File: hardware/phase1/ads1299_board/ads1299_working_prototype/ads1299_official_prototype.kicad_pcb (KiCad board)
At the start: 4 copper layers, 106 parts, among them J2 1725656, J3 TSM-110-01-T-DV-P-TR, J6 36PIN_IDC, J80 Conn_02x16_Odd_Even, J81 Conn_02x16_Odd_Even, J9 1725656, U1 ADS1299IPAG, U10 24AA256-I/ST, U11 OPA376AID, U4 OPA376

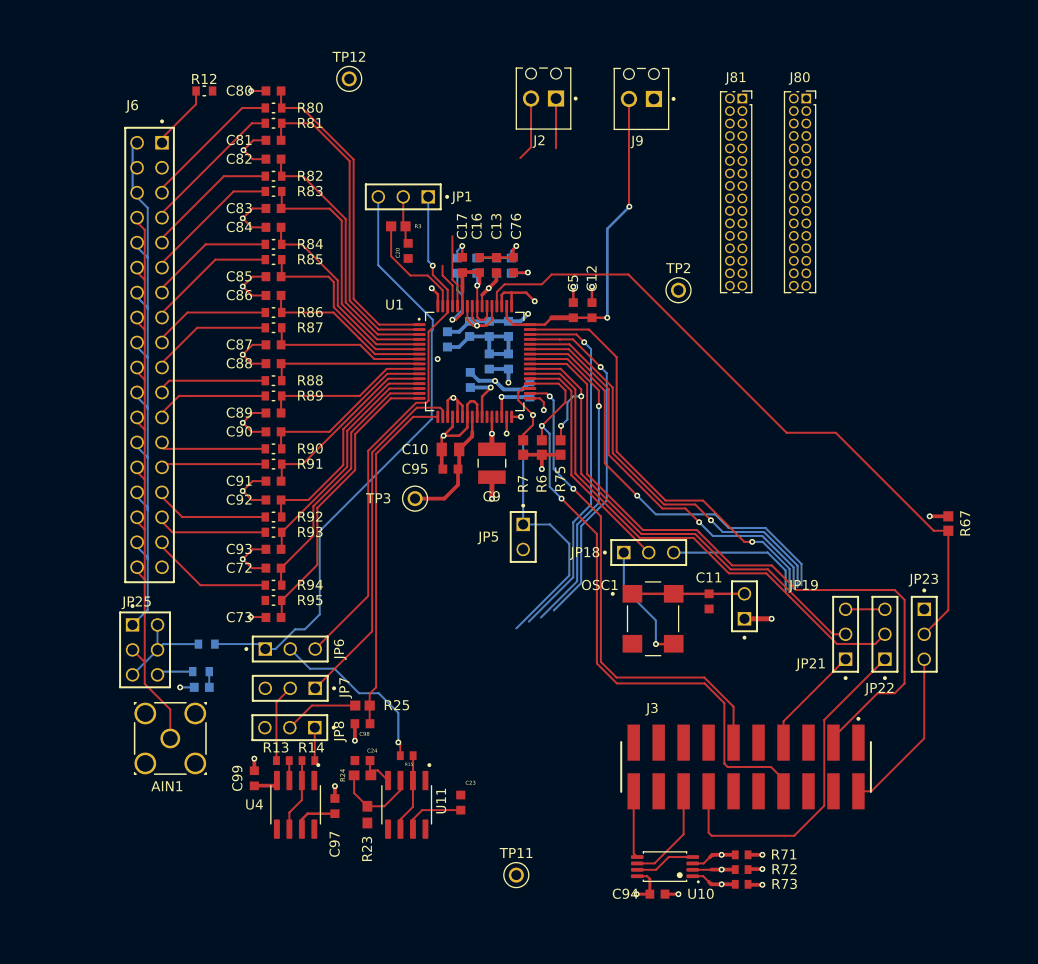
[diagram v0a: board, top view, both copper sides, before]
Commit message: Only thing left is the AVDD power routing, not sure if we can just connect that to power plane or not. Also ground plane, then done
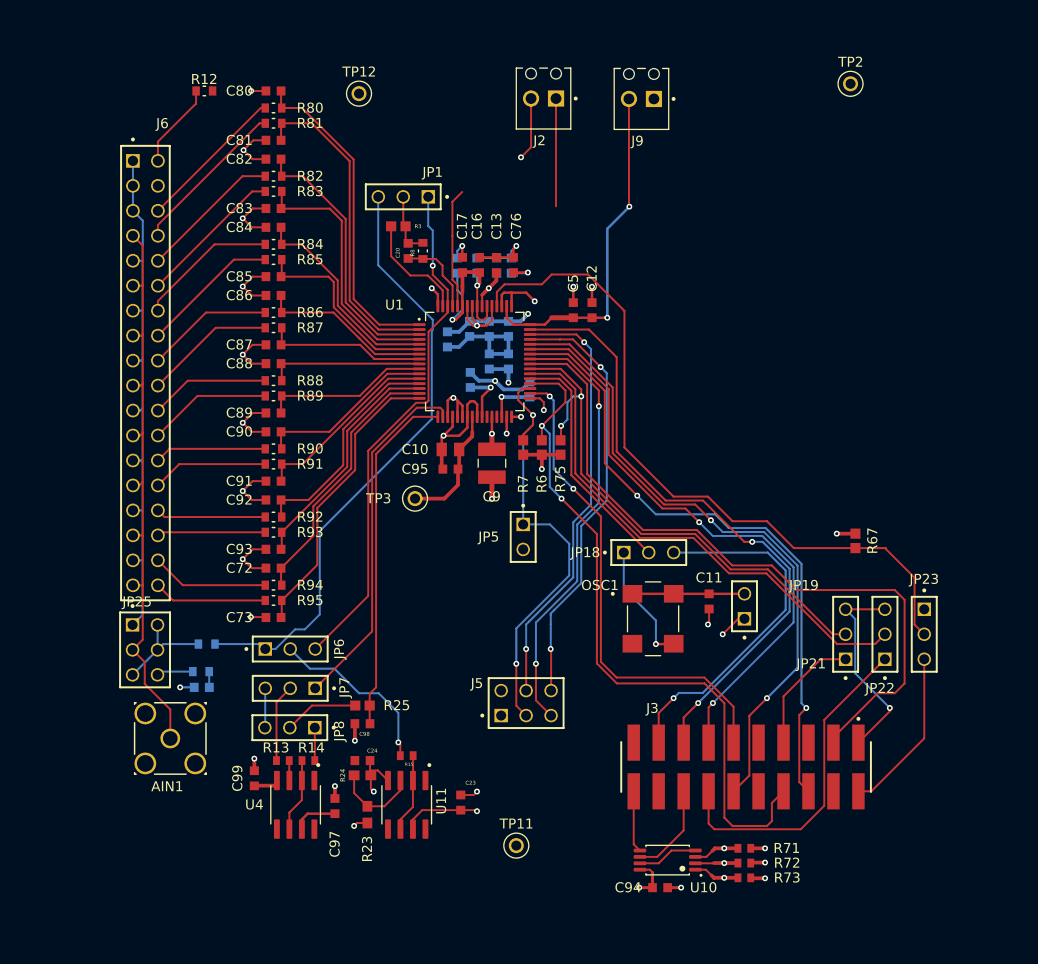
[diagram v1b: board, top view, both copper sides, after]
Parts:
- removed J80, J81: Conn_02x16_Odd_Even, Connector_PinSocket_1.27mm:PinSocket_2x16_P1.27mm_Vertical
- added J5: TSW-103-07-T-D, TSW-103-07-T-D:SAMTEC_TSW-103-07-T-D, F.Cu at (141.0, 109.5)
- added R8: 392K, RC0603FR-07392KL:RESC1608X55N, F.Cu at (130.5, 63.5)
- moved TP2 27.3 mm to (174.0, 46.5)
- moved R67 9.61 mm to (174.5, 93.0)
- moved TP11 3.00 mm to (140.0, 124.0)
- moved J6 2.42 mm to (102.4, 54.3)
- moved TP12 1.80 mm to (124.0, 47.5)
- moved U10 0.72 mm to (155.4, 125.5)
- moved C94 0.72 mm to (154.6, 128.3)
- moved R71 0.72 mm to (163.2, 124.3)
- moved R72 0.72 mm to (163.2, 125.8)
- moved R73 0.72 mm to (163.2, 127.3)
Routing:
- net GPIO2: track 42.6 -> 66.1 mm, vias 1 -> 2
- net EXT_CLK: track 14.3 -> 36.4 mm, vias 0 -> 1
- net GPIO1: track 42.9 -> 64.8 mm, vias 1 -> 2
- net SPI_DRDY: track 44.3 -> 64.3 mm, vias 1 -> 2
- net SPI_OUT: track 42.1 -> 61.3 mm, vias 1 -> 2
- net Net-(J3-Pad01): track 4.00 -> 20.8 mm, vias 0 -> 1
- net 36: track 0.00 -> 11.6 mm
- net 1: track 66.4 -> 55.3 mm
- net DAISY_IN: track 33.9 -> 44.7 mm, vias 1 -> 2
- net /PWDN: track 35.2 -> 44.4 mm, vias 1 -> 2
- net GPIO3: track 35.6 -> 43.9 mm, vias 1 -> 2
- net /RESET: track 66.2 -> 73.9 mm
- net AVSS: track 61.4 -> 69.1 mm, vias 7 -> 8
- net 11: track 68.6 -> 61.0 mm
- net GPIO4: track 37.2 -> 44.3 mm, vias 1 -> 2
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
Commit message: Planes are in, need to ask bruno on specifics about them then done
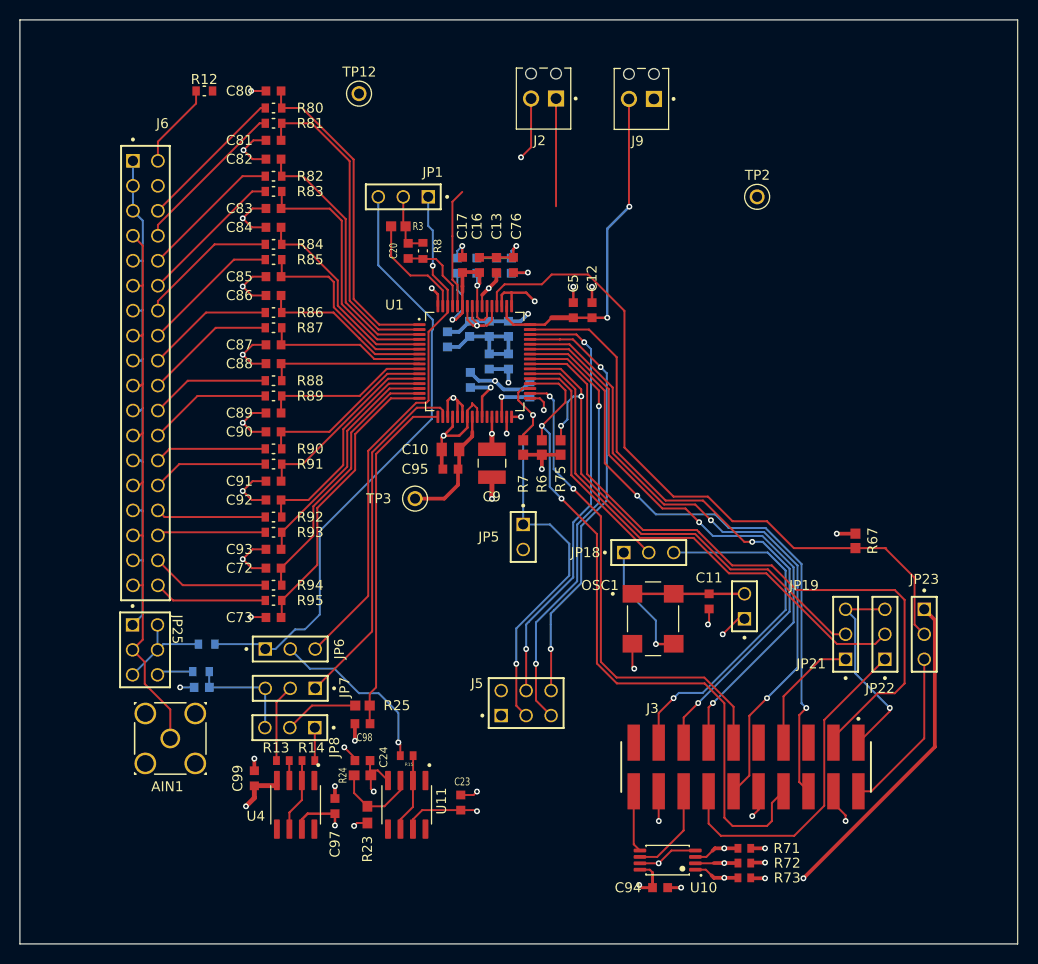
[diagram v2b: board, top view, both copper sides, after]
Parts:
- removed TP11: 5001, 5001:KEYSTONE_5001
- moved TP2 14.9 mm to (164.5, 58.0)
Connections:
- C94 pad 1: +3V3 -> DVDD
- R71 pad 2: +3V3 -> DVDD
- R72 pad 2: +3V3 -> DVDD
- R73 pad 2: +3V3 -> DVDD
- U10 pad 1: +3V3 -> DVDD
- U10 pad 2: +3V3 -> DVDD
- U10 pad 3: +3V3 -> DVDD
- U10 pad 8: +3V3 -> DVDD
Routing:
- net GND: track 11.9 -> 45.3 mm, vias 4 -> 6
- net DVDD: track 45.3 -> 63.4 mm, vias 5 -> 9
- net +3V3: track 18.0 -> 0.00 mm, vias 4 -> 0
- net GNDA: track 75.0 -> 89.0 mm, vias 24 -> 29
- net REF_ELEC: track 5.62 -> 11.4 mm
- net AVSS: track 69.1 -> 70.9 mm, vias 8 -> 9
- net AVDD: track 59.9 -> 61.1 mm, vias 6 -> 7
- net Net-(J3-Pad14): track 33.7 -> 34.3 mm
- added copper zone on In2.Cu, net DVDD
- added copper zone on In1.Cu, net GND
- added copper zone on In1.Cu, net GNDA
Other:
- board outline added: 101.5 x 94 mm

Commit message: DONE, but need to edit some footprints and add the biasref header
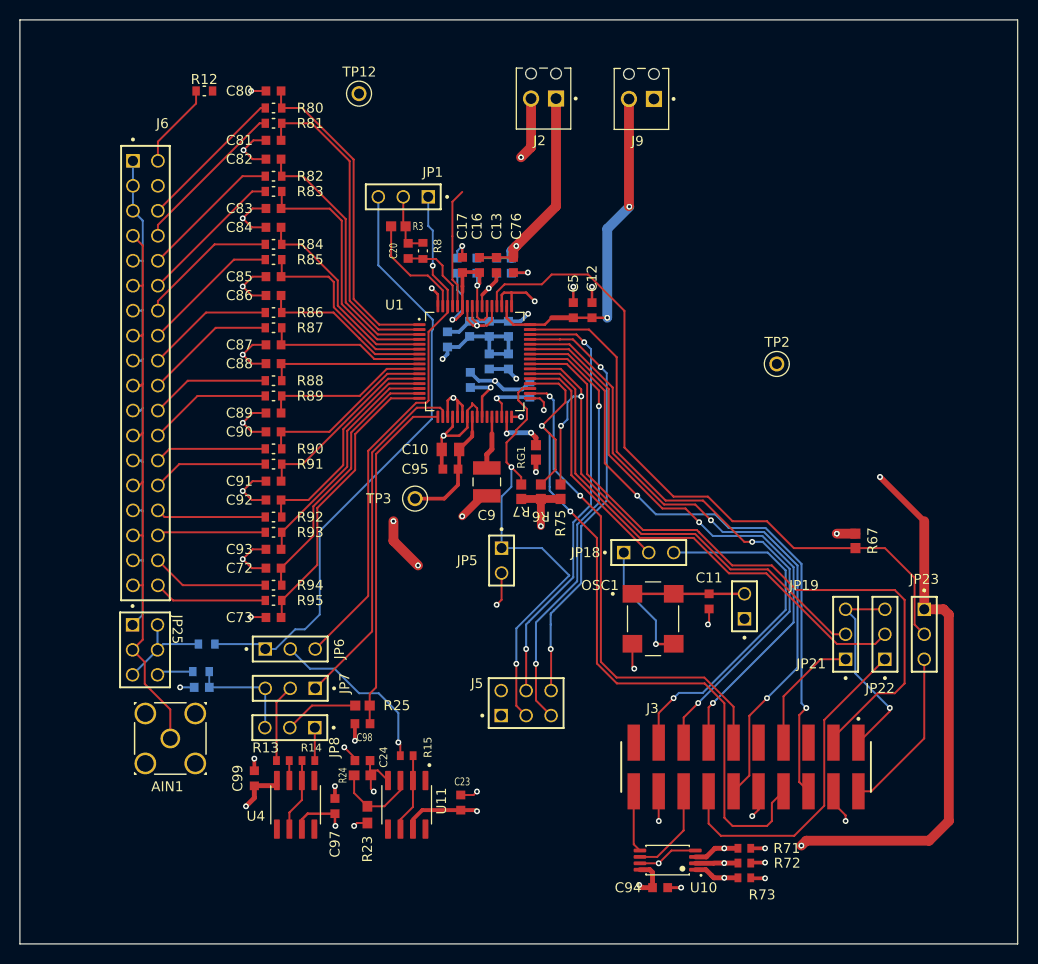
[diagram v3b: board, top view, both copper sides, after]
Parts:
- added RG1: 0, RC0603JR-070RL:RESC1607X60N, F.Cu at (142.0, 84.0)
- moved TP2 17.1 mm to (166.5, 75.0)
- moved R7 4.50 mm to (140.5, 88.0)
- moved R6 4.50 mm to (142.5, 88.0)
- moved R75 4.50 mm to (144.5, 88.0)
- moved JP5 3.26 mm to (138.5, 95.0)
- moved C9 1.97 mm to (137.0, 87.0)
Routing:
- net AVSS: track 70.9 -> 186.0 mm
- net DVDD: track 63.4 -> 168.4 mm, vias 9 -> 8
- net AVDD: track 61.1 -> 159.5 mm, vias 7 -> 10
- net GND: track 45.3 -> 103.5 mm, vias 6 -> 8
- net GNDA: track 89.0 -> 95.8 mm, vias 29 -> 31
- net /RESET: track 73.9 -> 79.6 mm
- net SPI_CS: track 54.1 -> 58.6 mm
- net VCAP1: track 3.30 -> 5.42 mm, vias 1 -> 0
- net /PWDN: track 44.4 -> 46.2 mm
- net VCAP2: track 4.92 -> 5.52 mm
- removed copper zone on In2.Cu, net DVDD

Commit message: Chat it's done
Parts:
- removed TP12: 5001, 5001:KEYSTONE_5001
- added JP60: TSW-103-07-T-S, TSW-103-07-T-S:SAMTEC_TSW-103-07-T-S, F.Cu at (133.0, 51.0)
- added REF**: MountingHole_2.2mm_M2, MountingHole:MountingHole_2.2mm_M2, F.Cu at (99.0, 48.0)
- added TPAVDD1: AVDD, 5000:KEYSTONE_5000, F.Cu at (135.5, 128.0)
- added TPAVSS1: AVSS, 5000:KEYSTONE_5000, F.Cu at (108.5, 126.0)
- added TPDVDD1: DVDD, 5000:KEYSTONE_5000, F.Cu at (173.0, 75.5)
- IC1: renamed from U1; value ADS1299IPAG -> ADS1299-4PAGR; footprint ADS1299CPAG:QFP64P50_1200X1200X120L60X22N -> KiCad:QFP50P1200X1200X120-64N
- moved TP2 22.0 mm to (162.0, 53.5)
- moved U4 0.65 mm to (117.5, 120.5)
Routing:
- net AVSS: track 186.0 -> 215.4 mm
- net AVDD: track 159.5 -> 174.3 mm
- net DVDD: track 168.4 -> 180.2 mm
- net SRB2: track 36.2 -> 44.9 mm
- net /PWDN: track 46.2 -> 39.3 mm
- net BIASREF: track 12.2 -> 18.5 mm, vias 0 -> 1
- net /RESET: track 79.6 -> 77.3 mm
- net Net-(U4--IN): track 7.50 -> 8.84 mm
- net Net-(U4-+IN): track 2.04 -> 2.69 mm
- net Net-(J3-Pad07): track 13.2 -> 12.6 mm
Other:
- board size 101.5 x 94 mm -> 96 x 91 mm

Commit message: Okay done
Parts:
- added REF**: MountingHole_2.2mm_M2, MountingHole:MountingHole_2.2mm_M2, F.Cu at (183.0, 128.0)
- added REF**: MountingHole_2.2mm_M2, MountingHole:MountingHole_2.2mm_M2, F.Cu at (99.0, 127.5)
- added REF**: MountingHole_2.2mm_M2, MountingHole:MountingHole_2.2mm_M2, F.Cu at (182.0, 48.0)
- FB1: renamed from RG1; value 0 -> FCM_1608KF-601T03; footprint RC0603JR-070RL:RESC1607X60N -> FCM_1608KF-601T03:BEADC1608X95N
- IC1: footprint KiCad:QFP50P1200X1200X120-64N -> ADS1299-4PAGR:QFP50P1200X1200X120-64N
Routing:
- net SRB2: track 44.9 -> 36.6 mm
